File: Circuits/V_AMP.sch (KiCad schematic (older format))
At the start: 43 parts, among them P1 INPUT, P2 GAIN_ADJ, P3 OUTPUT (0-5V), P4 +8, P5 -8, P6 GND, U1 OPA177, U2 LM393, U3 OPA177

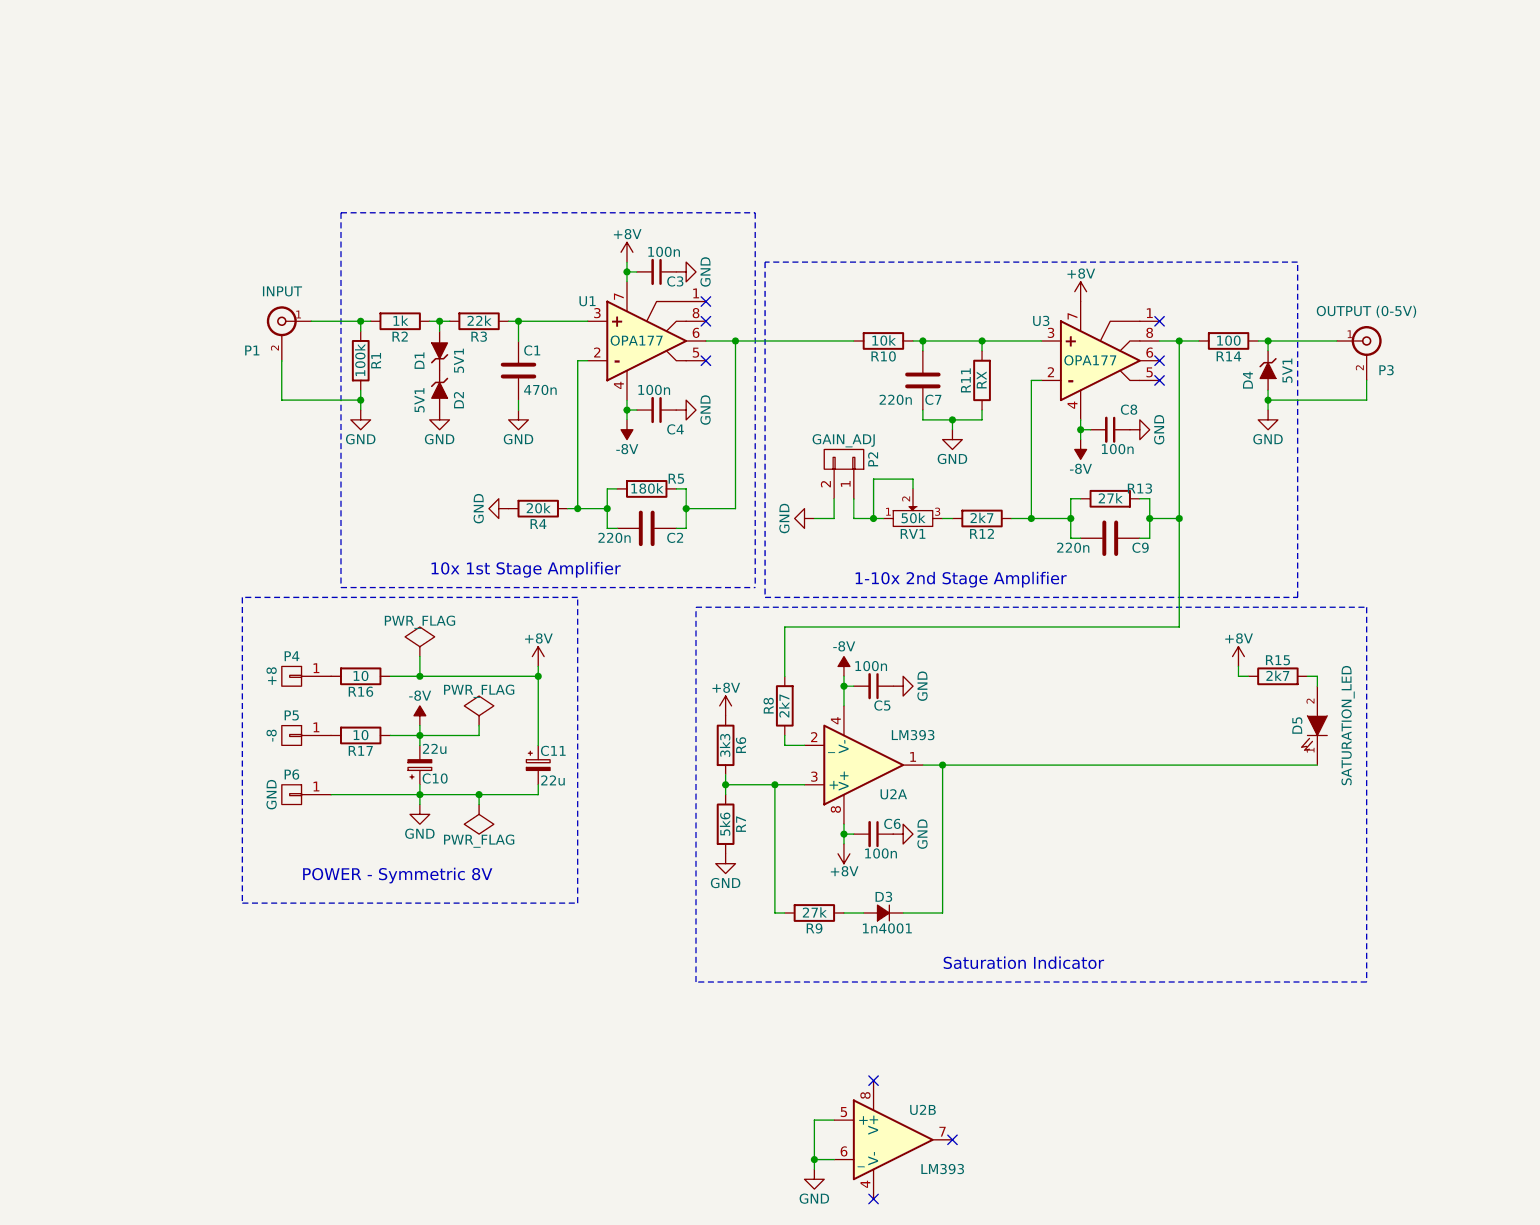
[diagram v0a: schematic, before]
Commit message: ADD: Schematic Documentation
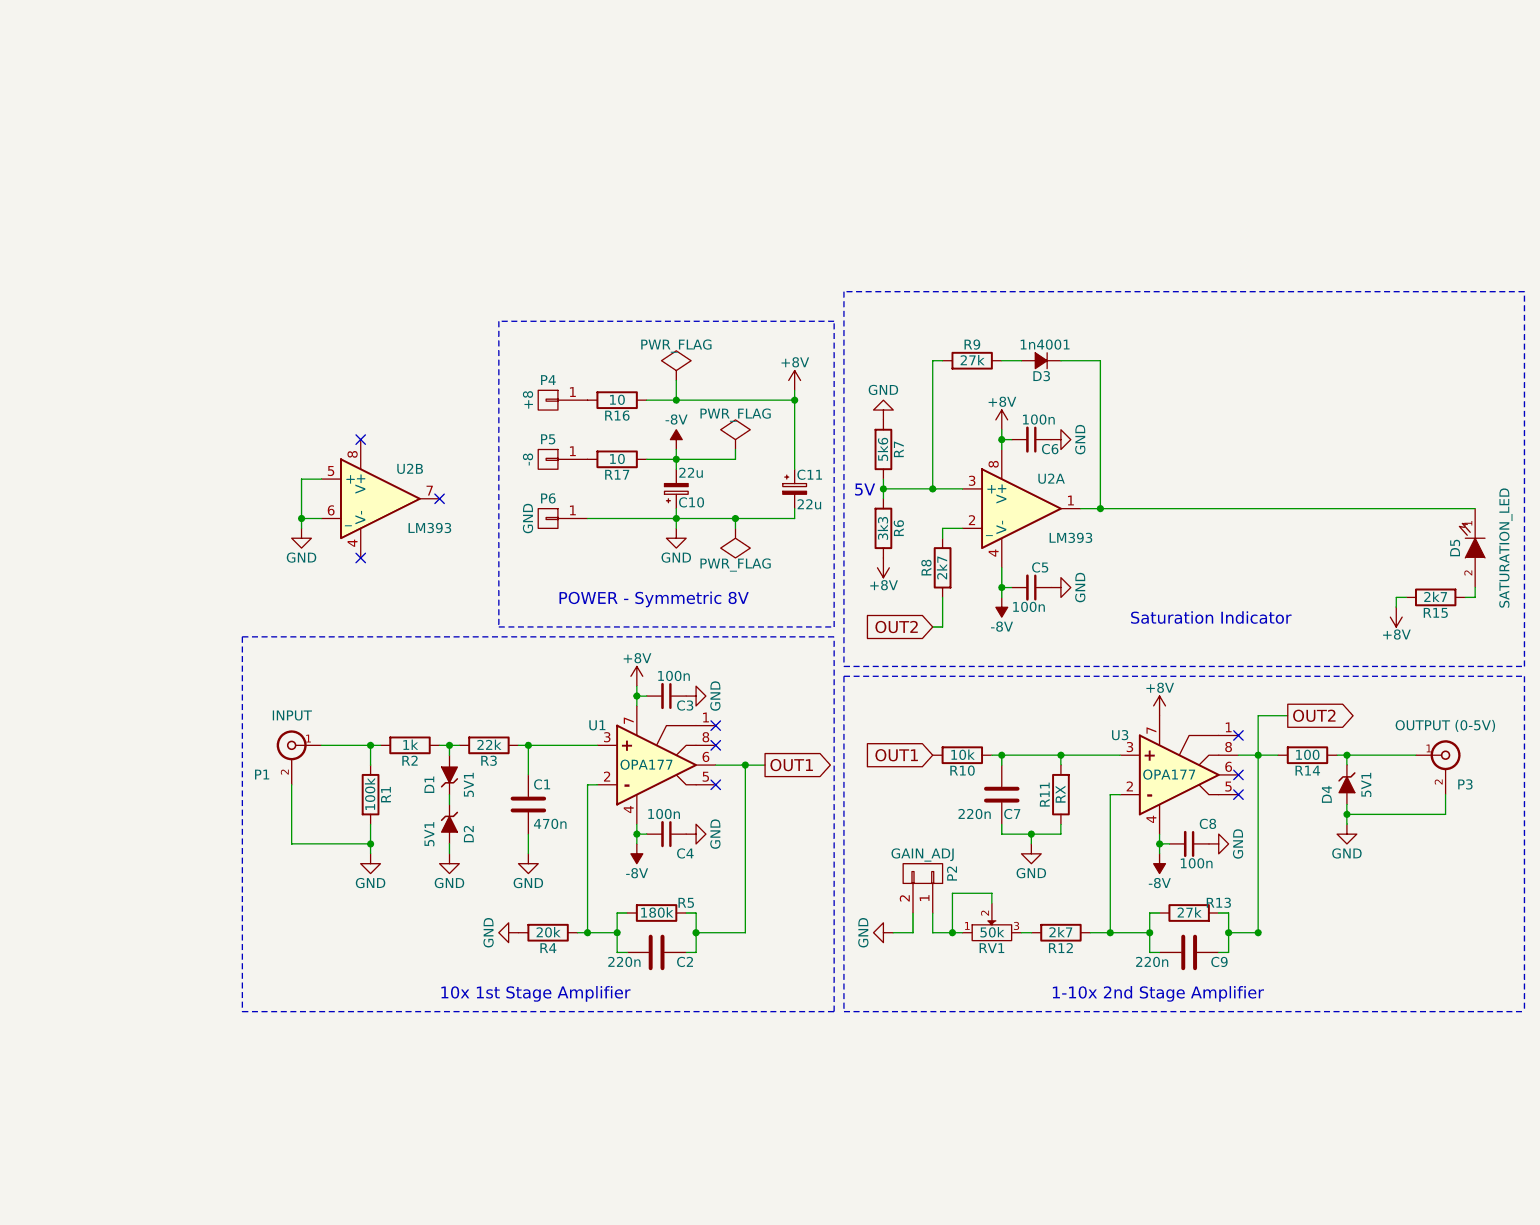
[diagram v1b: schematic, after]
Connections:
- net OUT1: now reaches C2.1, R10.2, R5.1, U1.6 (OUTPUT)
- net OUT2: now reaches C9.2, R13.2, R14.2, R8.2, U3.8 (COMP)
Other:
- note added: "5V"
- moved on the sheet: C1, C10, C11, C2, C3, C4, C5, C6, C7, C8, C9, D1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

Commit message: Complete PCB Design of the PreAmp 10-100
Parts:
- removed P4: +8, symbol CONN_01X01
- removed P5: -8, symbol CONN_01X01
- removed P6: GND, symbol CONN_01X01
- added P4: POWER, Connectors:bornier3, symbol CONN_01X03
- C1, C2, C3, C4, C5, C6, C7, C8, C9: footprint (none) -> Capacitors_THT:C_Rect_L7.0mm_W2.5mm_P5.00mm
- C10, C11: footprint (none) -> Capacitors_THT:CP_Radial_D5.0mm_P2.50mm
- D1, D2, D4: footprint (none) -> Diodes_THT:D_DO-41_SOD81_P7.62mm_Horizontal
- D3: value 1n4001 -> 1N4148; footprint (none) -> Diodes_THT:D_DO-35_SOD27_P7.62mm_Horizontal
- D5: footprint (none) -> LEDs:LED_D5.0mm
- P1, P3: footprint (none) -> Connectors:bnc-ci
- P2: footprint (none) -> w_pin_strip:pin_strip_2mm_2
- R1, R10, R11, R12, R13, R14, R15, R16, R17, R2, R3, R4, R5, R6, R7, R8, R9: footprint (none) -> w_pth_resistors:RC03
- RV1: footprint (none) -> Potentiometers:Potentiometer_Alps_RK163_Single_Vertical
- U1, U2, U3: footprint (none) -> Housings_DIP:DIP-8_W7.62mm_Socket_LongPads
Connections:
- net GND: now also P4.1 (P1)
- net OUT2: now also U3.6 (OUTPUT); no longer U3.8 (COMP)
- net at R16.2: now also P4.3 (P3)
- net at R17.2: now also P4.2 (P2)
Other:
- note added: "+8"
- note added: "-8\n"
- note added: "1W"
- note added: "GND"
- moved on the sheet: D4, P3, R14, R16, R17

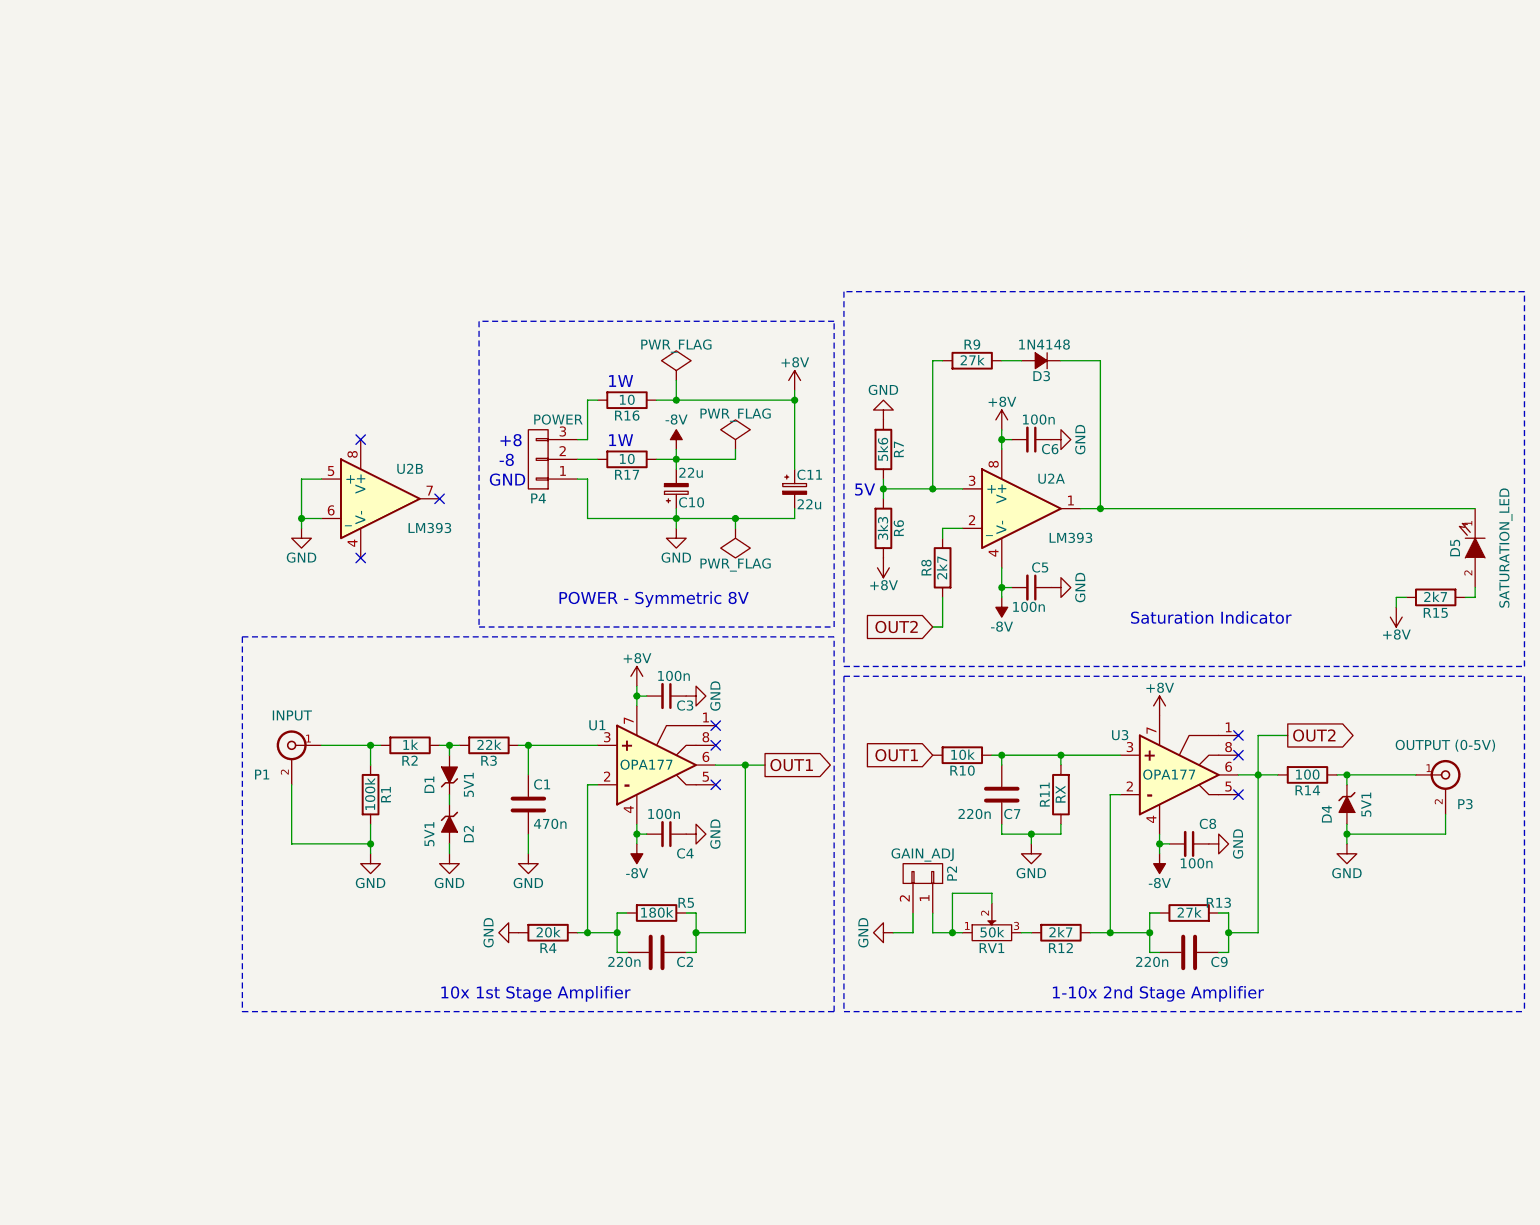
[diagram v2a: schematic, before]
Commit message: Added full schematics and power supply
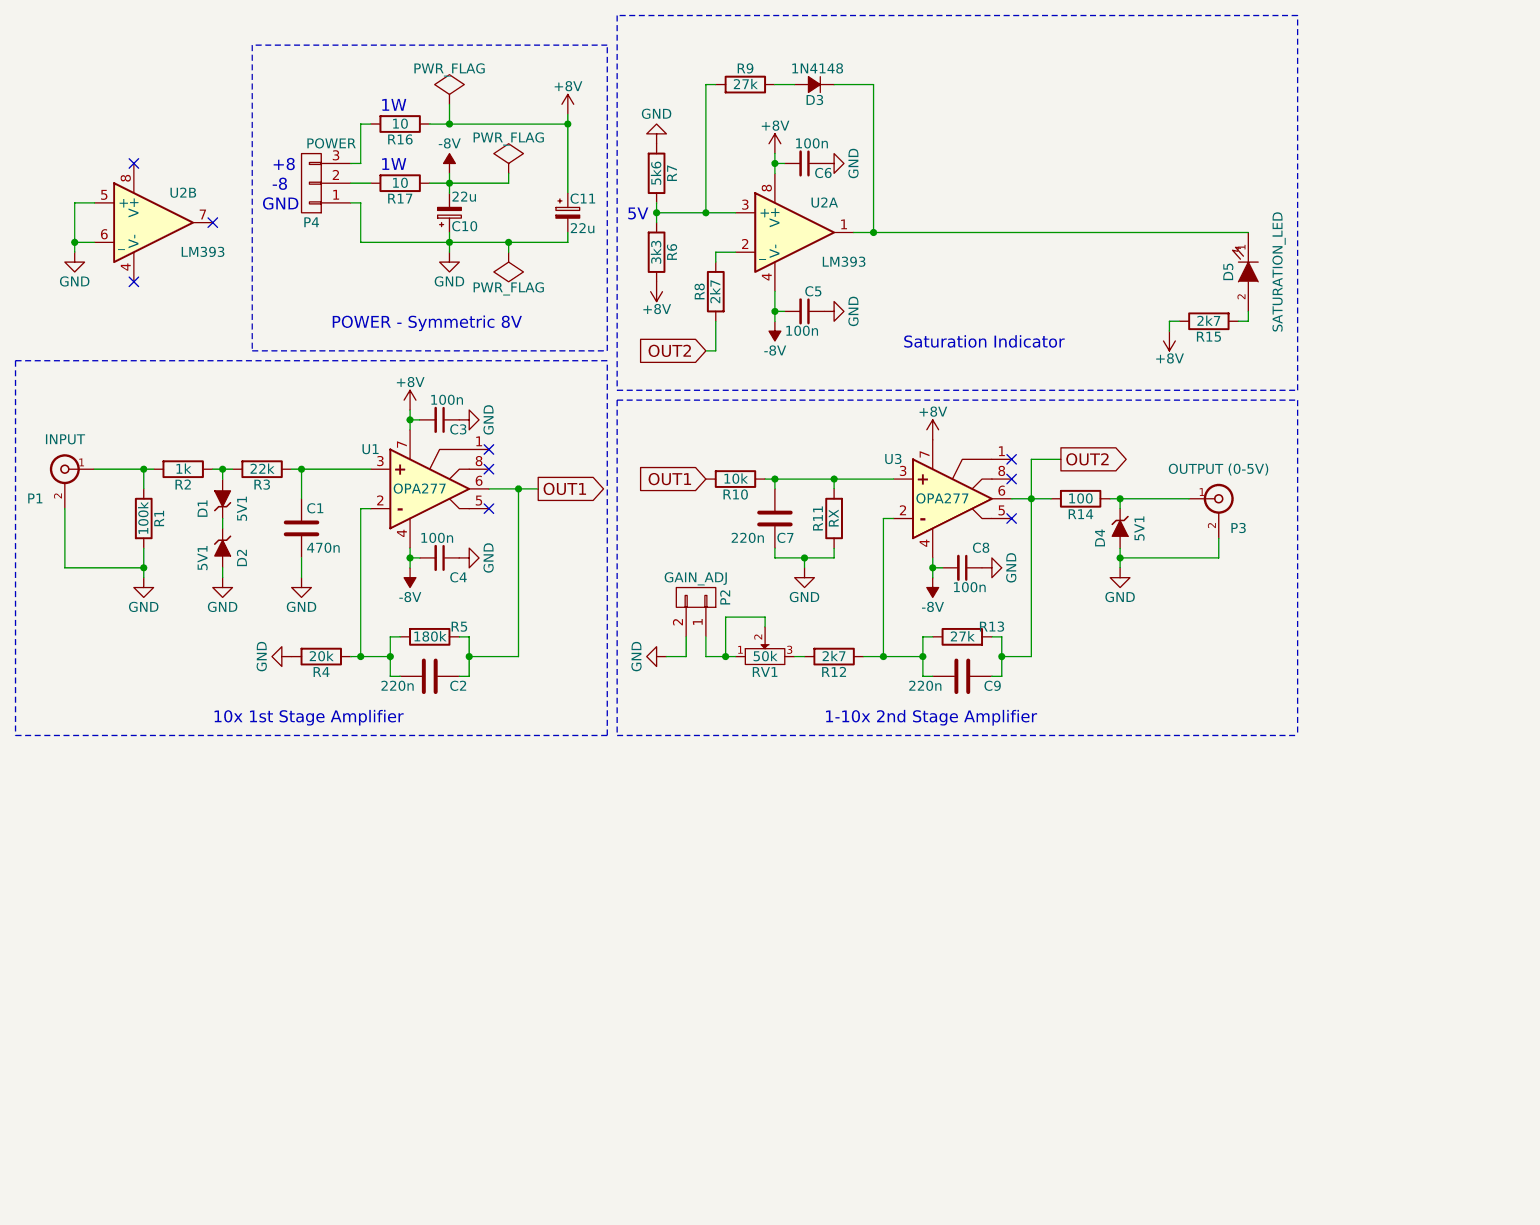
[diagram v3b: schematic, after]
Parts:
- U1, U3: value OPA177 -> OPA277
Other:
- moved on the sheet: C1, C10, C11, C2, C3, C4, C5, C6, C7, C8, C9, D1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
